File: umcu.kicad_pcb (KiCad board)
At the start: 4 copper layers, 5.1 x 5.1 mm, 8 parts, among them J1 Conn_02x02_Odd_Even

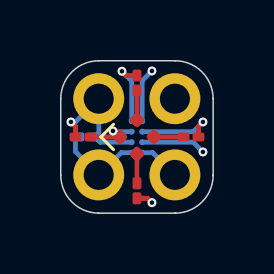
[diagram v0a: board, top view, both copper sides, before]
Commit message: switch design to 2L board
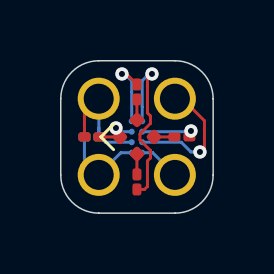
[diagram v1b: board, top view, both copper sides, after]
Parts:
- moved R2 0.30 mm to (132.3, 100.3)
- moved R4 0.30 mm to (129.3, 100.3)
- moved R1 0.30 mm to (130.8, 98.8)
- moved R3 0.30 mm to (130.8, 101.8)
- moved C1 0.20 mm to (129.3, 100.3)
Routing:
- net /LED_G: track 2.97 -> 1.70 mm
- net /LED_B: track 7.69 -> 6.49 mm, vias 2 -> 1
- net +3.3V: track 4.48 -> 4.03 mm, vias 1 -> 0
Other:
- copper layers 4 -> 2
